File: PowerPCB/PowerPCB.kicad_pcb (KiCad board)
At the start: 2 copper layers, 25 parts, among them J1 Conn_01x03_Male, J2 Conn_01x08_Male, J3 STM Inputs, J4 STM Outputs, J5 Conn_01x07_Male, K1 HF3-06, K3 ALFG2PF121, Q1 Q_PMOS_DGS, U1 NCP1117-3.3_SOT223, U2 STM32F413ZHTx

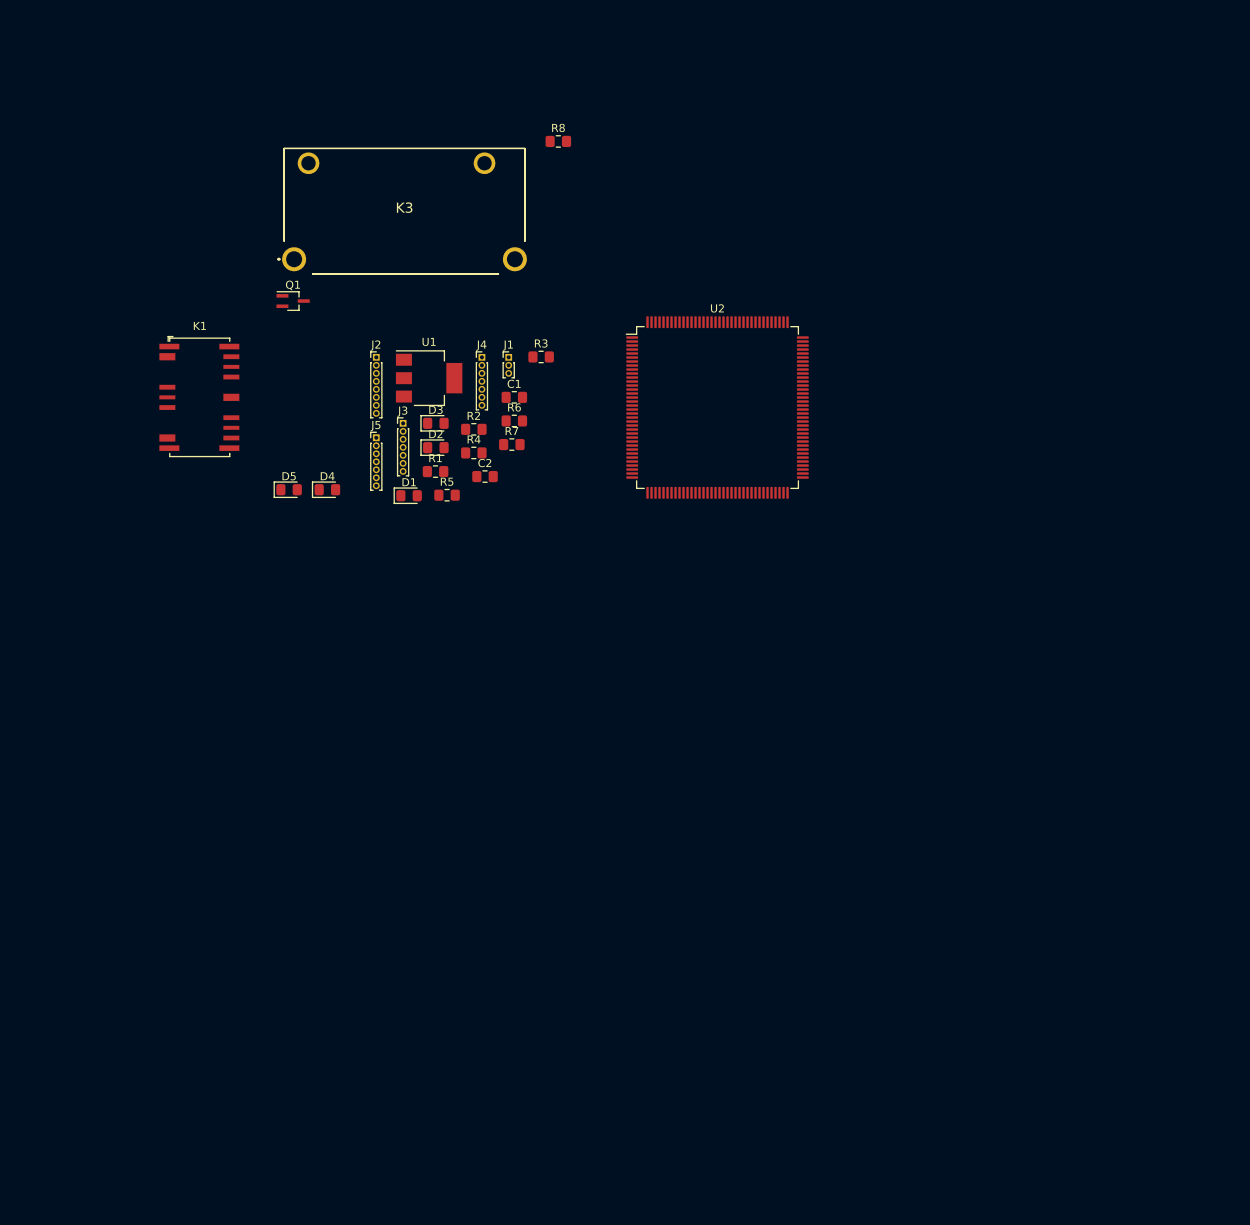
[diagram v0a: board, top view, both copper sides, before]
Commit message: Added CAN connections to STM
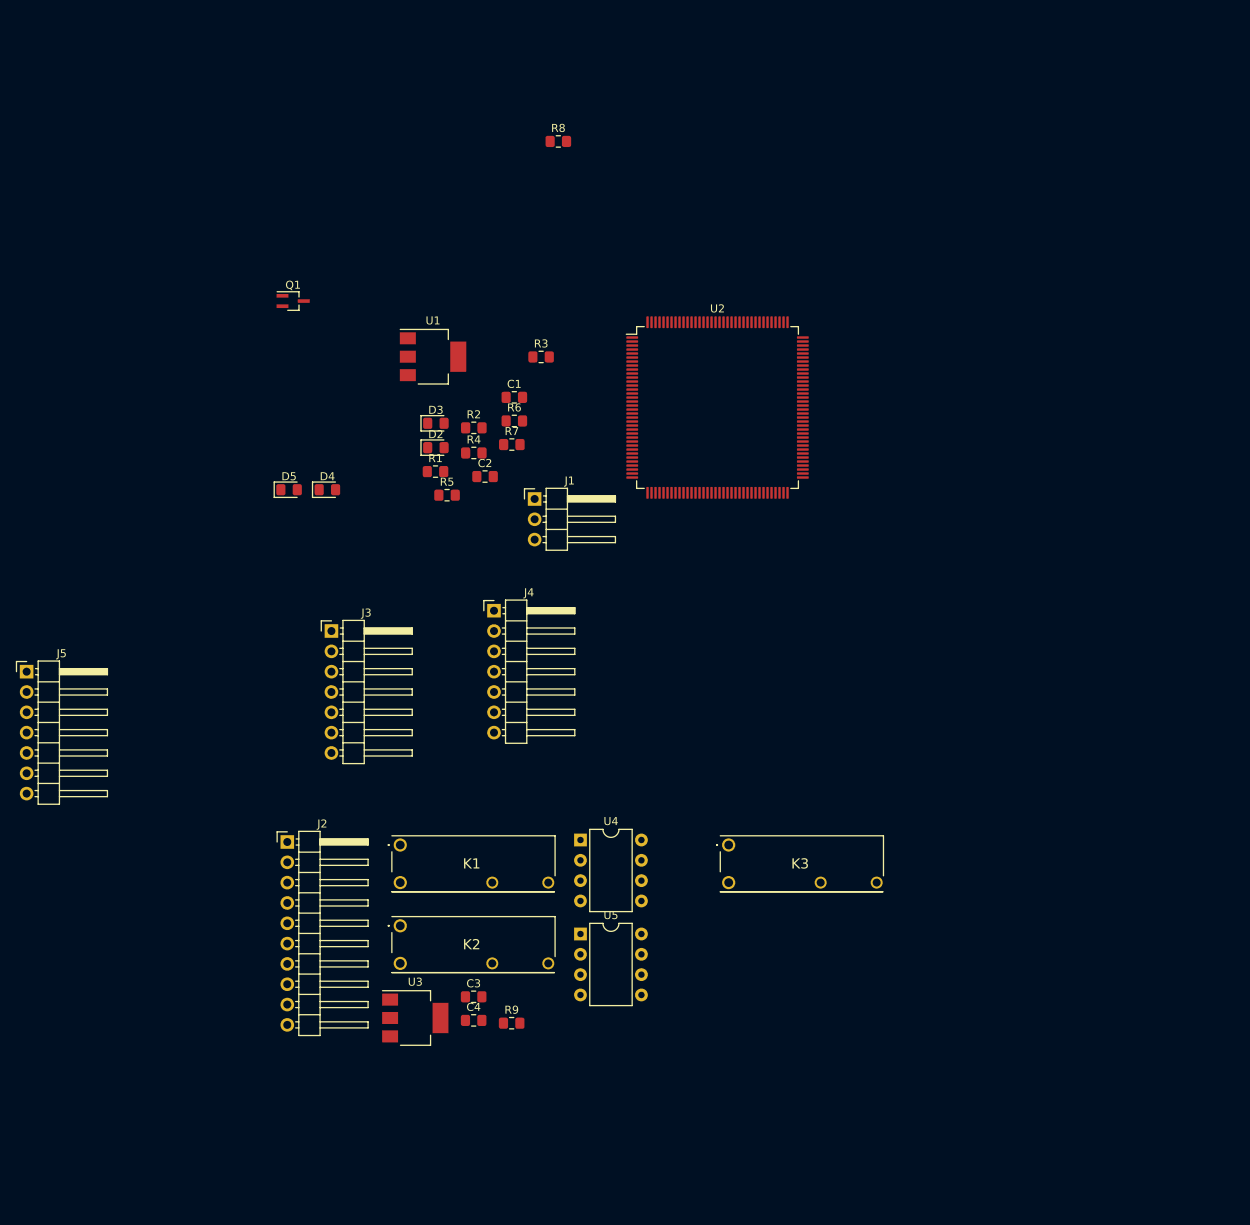
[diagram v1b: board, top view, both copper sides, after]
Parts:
- removed D1: DIODE, Diode_SMD:D_0805_2012Metric_Pad1.15x1.40mm_HandSolder
- added C3: C, Capacitor_SMD:C_0805_2012Metric_Pad1.15x1.40mm_HandSolder, F.Cu at (355.6, 254.0)
- added C4: C, Capacitor_SMD:C_0805_2012Metric_Pad1.15x1.40mm_HandSolder, F.Cu at (355.6, 256.9)
- added K2: 1721081-5, SamacSys_Parts:17210815, F.Cu at (346.4, 245.1)
- added R9: 120, Resistor_SMD:R_0805_2012Metric_Pad1.15x1.40mm_HandSolder, F.Cu at (360.4, 257.3)
- added U3: NCP1117-5.0_SOT223, Package_TO_SOT_SMD:SOT-223-3_TabPin2, F.Cu at (348.3, 256.6)
- added U4: MCP2562-E-P, Package_DIP:DIP-8_W7.62mm, F.Cu at (368.9, 234.4)
- added U5: MCP2562-E-P, Package_DIP:DIP-8_W7.62mm, F.Cu at (368.9, 246.2)
- J1: footprint Connector_PinHeader_1.00mm:PinHeader_1x03_P1.00mm_Vertical -> Connector_PinHeader_2.54mm:PinHeader_1x03_P2.54mm_Horizontal
- J2: value Conn_01x08_Male -> Conn_01x10_Male; footprint Connector_PinHeader_1.00mm:PinHeader_1x08_P1.00mm_Vertical -> Connector_PinHeader_2.54mm:PinHeader_1x10_P2.54mm_Horizontal
- J3, J4, J5: footprint Connector_PinHeader_1.00mm:PinHeader_1x07_P1.00mm_Vertical -> Connector_PinHeader_2.54mm:PinHeader_1x07_P2.54mm_Horizontal
- K1: value HF3-06 -> 1721081-5; footprint Relay_SMD:Relay_SPDT_AXICOM_HF3Series_75ohms_Pitch1.27mm -> SamacSys_Parts:17210815
- K3: value ALFG2PF121 -> 1721081-5; footprint SamacSys_Parts:ALFG2PF121 -> SamacSys_Parts:17210815
- R3: value R -> 120
- moved K3 91.2 mm to (387.5, 235.0)
- moved J2 61.6 mm to (332.3, 234.7)
- moved K1 61.3 mm to (346.4, 235.0)
- moved J5 52.6 mm to (299.7, 213.4)
- moved J4 31.7 mm to (358.1, 205.7)
- moved J3 27.5 mm to (337.8, 208.3)
- moved J1 18.0 mm to (363.2, 191.8)
- moved U1 2.72 mm to (350.5, 174.0)
- moved R2 0.19 mm to (355.6, 182.9)
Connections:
- net Net-(C2-Pad1) renamed VCC_3.3
- J1 pad 1: Net-(J1-Pad1) -> BMS_CAN_HI
- J1 pad 2: Net-(J1-Pad2) -> BMS_CAN_LO
- J2 pad 2: GND -> Net-(J2-Pad2)
- J2 pad 3: Net-(D1-Pad1) -> VCC_12
- J3 pad 1: Net-(J1-Pad1) -> Net-(J3-Pad1)
- J3 pad 2: Net-(J1-Pad2) -> Net-(J3-Pad2)
- J3 pad 5: Net-(D1-Pad1) -> Net-(J2-Pad2)
- J5 pad 1: VCC_12 -> /Fan/Fan+
- J5 pad 2: GND -> /Fan/Fan-
- J5 pad 3: /Fan/Fan+ -> MAIN_CAN_HI
- J5 pad 4: /Fan/Fan- -> MAIN_CAN_LO
- K1 pad 1: Net-(D1-Pad1) -> VCC_12
- K1 pad 2: GND -> Net-(J2-Pad7)
- K3 pad 1: /Fan/Fan- -> VCC_12
- K3 pad 2: GND -> /Fan/FanCtrl
- K3 pad 3: /Fan/FanCtrl -> GND
- K3 pad 4: VCC_12 -> /Fan/Fan-
- R3 pad 1: Net-(J1-Pad1) -> BMS_CAN_HI
- R3 pad 2: Net-(J1-Pad2) -> BMS_CAN_LO
- U2 pad 114: Net-(U2-Pad114) -> BMS_CAN_RX
- U2 pad 115: Net-(U2-Pad115) -> BMS_CAN_TX
- U2 pad 73: Net-(U2-Pad73) -> MAIN_CAN_RX
- U2 pad 74: Net-(U2-Pad74) -> MAIN_CAN_TX

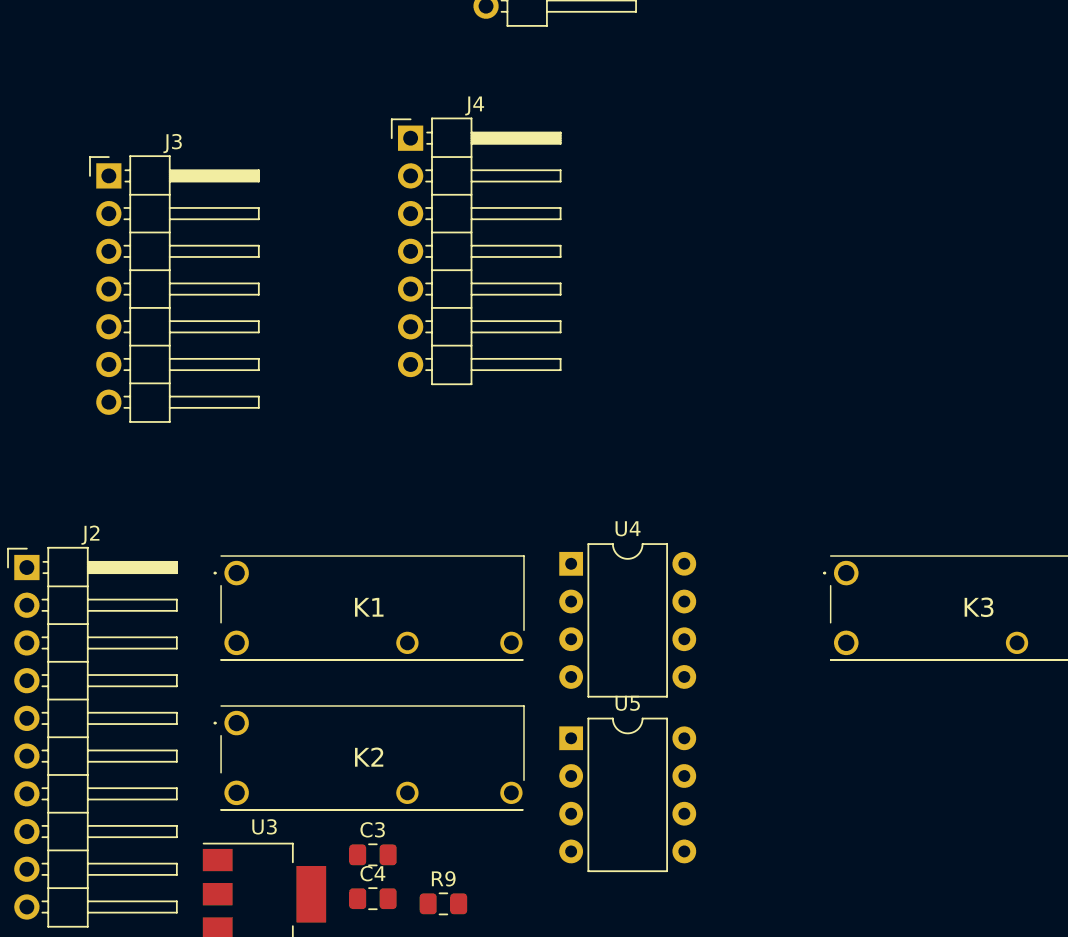
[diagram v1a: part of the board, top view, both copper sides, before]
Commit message: Added AUX+ and DCDC+ as analog inputs
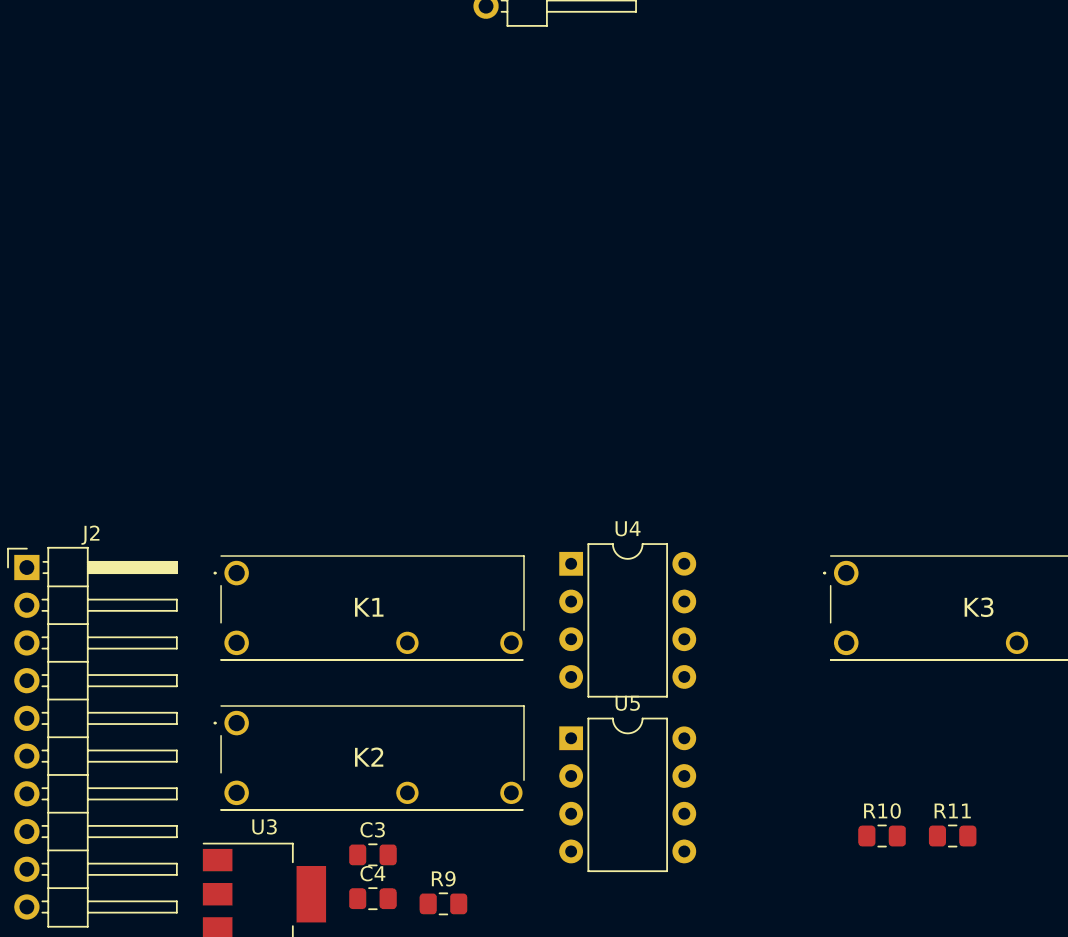
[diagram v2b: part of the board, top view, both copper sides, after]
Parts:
- removed J3: STM Inputs, Connector_PinHeader_2.54mm:PinHeader_1x07_P2.54mm_Horizontal
- removed J4: STM Outputs, Connector_PinHeader_2.54mm:PinHeader_1x07_P2.54mm_Horizontal
- added R10: 100k, Resistor_SMD:R_0805_2012Metric_Pad1.15x1.40mm_HandSolder, F.Cu at (389.9, 252.7)
- added R11: 33k, Resistor_SMD:R_0805_2012Metric_Pad1.15x1.40mm_HandSolder, F.Cu at (394.6, 252.7)
- R1: value R -> 100k
- R2: value R -> 33k
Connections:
- J2 pad 1: Net-(J2-Pad1) -> AUX+
- J2 pad 2: Net-(J2-Pad2) -> DCDC+
- R1 pad 1: Net-(J3-Pad4) -> AUX+
- R1 pad 2: GND -> Net-(R1-Pad2)
- R2 pad 1: Net-(J3-Pad4) -> Net-(R1-Pad2)
- R2 pad 2: Net-(J2-Pad1) -> GND
- R4 pad 1: Net-(J4-Pad7) -> Net-(R4-Pad1)
- R5 pad 1: Net-(J4-Pad6) -> Net-(R5-Pad1)
- R6 pad 1: Net-(J4-Pad5) -> Net-(R6-Pad1)
- R7 pad 1: Net-(J4-Pad4) -> VCC_3.3
- U2 pad 137: Net-(U2-Pad137) -> Net-(R5-Pad1)
- U2 pad 37: Net-(U2-Pad37) -> Net-(R1-Pad2)
- U2 pad 46: Net-(U2-Pad46) -> Net-(R4-Pad1)
- U2 pad 75: Net-(U2-Pad75) -> Net-(R6-Pad1)

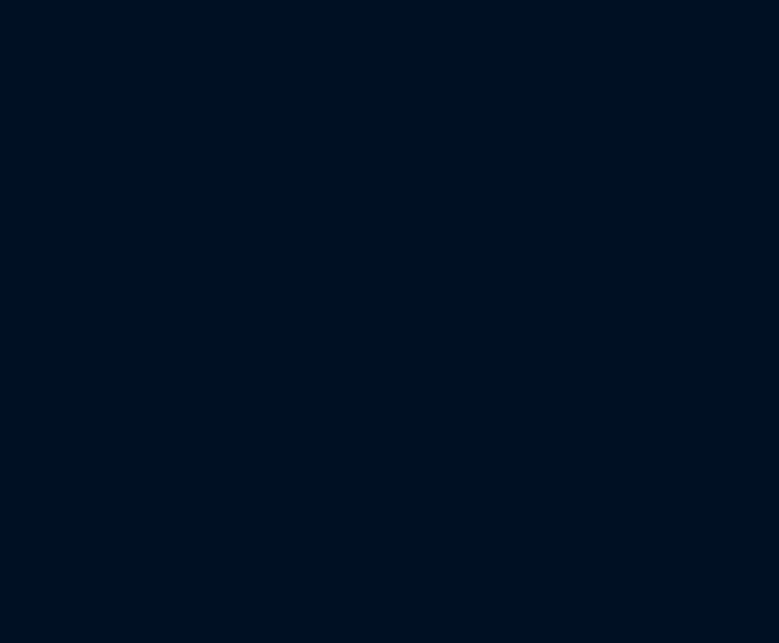
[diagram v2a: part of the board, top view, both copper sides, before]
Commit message: Finished connections to STM, exported to PCBnew
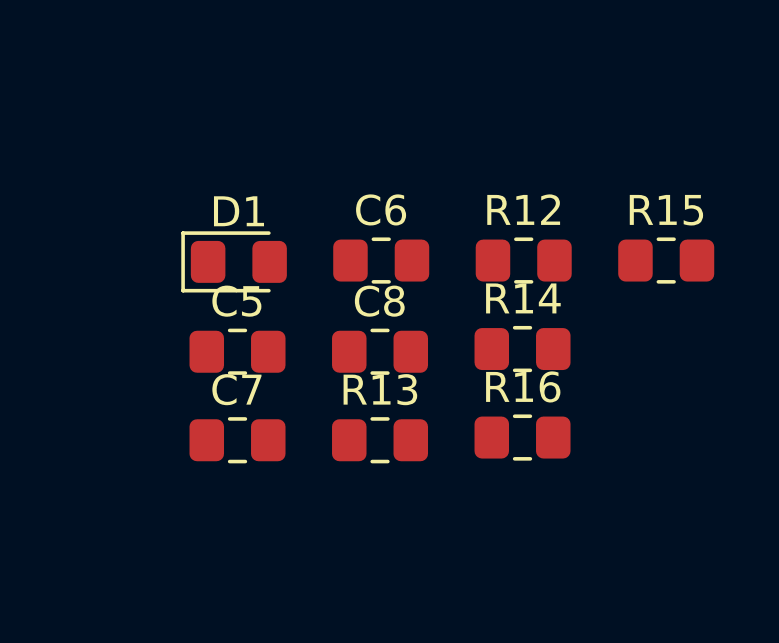
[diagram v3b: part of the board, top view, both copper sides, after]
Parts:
- added C5: C, Capacitor_SMD:C_0805_2012Metric_Pad1.15x1.40mm_HandSolder, F.Cu at (402.6, 221.0)
- added C6: 2.2u, Capacitor_SMD:C_0805_2012Metric_Pad1.15x1.40mm_HandSolder, F.Cu at (407.4, 217.9)
- added C7: 2.2u, Capacitor_SMD:C_0805_2012Metric_Pad1.15x1.40mm_HandSolder, F.Cu at (402.6, 223.9)
- added C8: 100n, Capacitor_SMD:C_0805_2012Metric_Pad1.15x1.40mm_HandSolder, F.Cu at (407.3, 221.0)
- added D1: LED, LED_SMD:LED_0805_2012Metric_Pad1.15x1.40mm_HandSolder, F.Cu at (402.6, 218.0)
- added R12: 100k, Resistor_SMD:R_0805_2012Metric_Pad1.15x1.40mm_HandSolder, F.Cu at (412.1, 217.9)
- added R13: 100k, Resistor_SMD:R_0805_2012Metric_Pad1.15x1.40mm_HandSolder, F.Cu at (407.3, 223.9)
- added R14: 33k, Resistor_SMD:R_0805_2012Metric_Pad1.15x1.40mm_HandSolder, F.Cu at (412.1, 220.9)
- added R15: R, Resistor_SMD:R_0805_2012Metric_Pad1.15x1.40mm_HandSolder, F.Cu at (416.9, 217.9)
- added R16: 40k, Resistor_SMD:R_0805_2012Metric_Pad1.15x1.40mm_HandSolder, F.Cu at (412.1, 223.8)
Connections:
- J2 pad 1: AUX+ -> DCDC_ON
- J2 pad 2: DCDC+ -> AUX+
- J2 pad 3: VCC_12 -> DCDC+
- J2 pad 4: GND -> VCC_12
- J2 pad 5: /Fan/FanPWM -> GND
- J2 pad 6: /Fan/FanCtrl -> /Fan/FanPWM
- J2 pad 7: Net-(J2-Pad7) -> /Fan/FanCtrl
- K1 pad 2: Net-(J2-Pad7) -> Net-(J2-Pad8)
- K1 pad 3: Net-(J2-Pad9) -> Net-(J2-Pad10)
- K2 pad 2: Net-(J2-Pad8) -> Net-(J2-Pad9)
- U2 pad 107: Net-(U2-Pad107) -> GND
- U2 pad 108: Net-(U2-Pad108) -> VCC_3.3
- U2 pad 120: Net-(U2-Pad120) -> GND
- U2 pad 121: Net-(U2-Pad121) -> VCC_3.3
- U2 pad 130: Net-(U2-Pad130) -> GND
- U2 pad 131: Net-(U2-Pad131) -> VCC_3.3
- U2 pad 138: Net-(U2-Pad138) -> GND
- U2 pad 143: Net-(U2-Pad143) -> VCC_3.3
- U2 pad 144: Net-(U2-Pad144) -> VCC_3.3
- U2 pad 16: Net-(U2-Pad16) -> GND
- U2 pad 17: Net-(U2-Pad17) -> VCC_3.3
- U2 pad 30: Net-(U2-Pad30) -> VCC_3.3
- U2 pad 31: Net-(U2-Pad31) -> GND
- U2 pad 32: Net-(U2-Pad32) -> VCC_3.3
- U2 pad 33: Net-(U2-Pad33) -> VCC_3.3
- U2 pad 38: Net-(U2-Pad38) -> GND
- U2 pad 39: Net-(U2-Pad39) -> VCC_3.3
- U2 pad 51: Net-(U2-Pad51) -> GND
- U2 pad 52: Net-(U2-Pad52) -> VCC_3.3
- U2 pad 6: Net-(U2-Pad6) -> VCC_3.3
- U2 pad 61: Net-(U2-Pad61) -> GND
- U2 pad 62: Net-(U2-Pad62) -> VCC_3.3
- U2 pad 72: Net-(U2-Pad72) -> VCC_3.3
- U2 pad 83: Net-(U2-Pad83) -> GND
- U2 pad 84: Net-(U2-Pad84) -> VCC_3.3
- U2 pad 94: Net-(U2-Pad94) -> GND
